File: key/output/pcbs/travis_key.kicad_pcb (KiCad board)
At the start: 2 copper layers, 38.1 x 38.1 mm, 4 parts

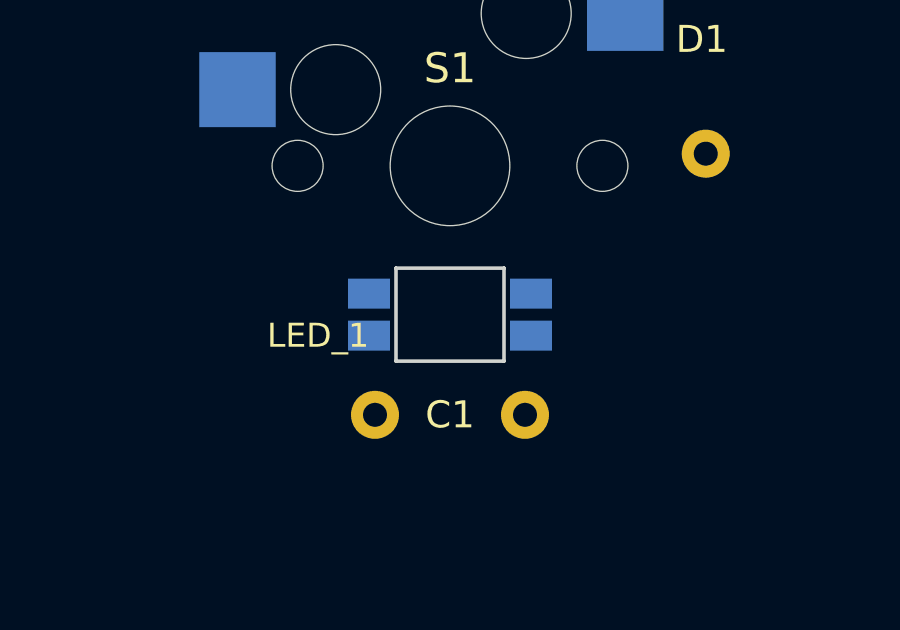
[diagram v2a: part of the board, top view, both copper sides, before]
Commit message: rtl option added
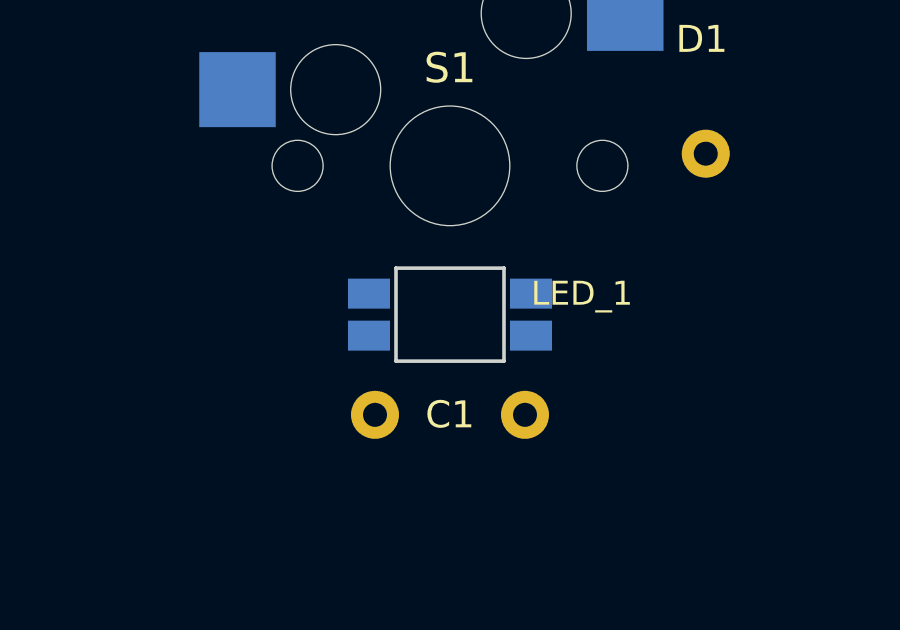
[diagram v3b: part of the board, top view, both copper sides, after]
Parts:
- moved C1 5.00 mm to (-2.50, 8.30), turned to 0 degrees
- turned LED1 to 180 degrees
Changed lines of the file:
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@@
       (module "ceoloide:led_SK6812mini-e (per-key single-side)"
         (layer B.Cu)
-        (at 0 4.96 0)
-        (fp_text reference "LED1" (at -5.25 0 90) (layer B.SilkS)
+        (at 0 4.96 180)
+        (fp_text reference "LED1" (at -4.75 0 270) (layer B.SilkS)
           (effects (font (size 1 1) (thickness 0.15)) (justify  mirror))
         )
-        (fp_text value "SK6812mini-e" (at 0 -2.25 0) (layer "B.Fab")
+        (fp_text value "SK6812mini-e" (at 0 2.25 180) (layer "B.Fab")
           (effects (font (size 0.8 0.8) (thickness 0.15)))
         )
@@
         (fp_line (start -3.8 0) (end -3.8 -1.6) (layer B.SilkS) (width 0.12))
         (fp_line (start -3.8 -1.36) (end -3.56 -1.6) (layer B.SilkS) (width 0.12))
-        (pad 2 smd rect (at 2.70 -0.7 0) (size 1.4 1) (layers B.Cu B.Paste B.Mask) (net 5 "LED_2"))
-        (pad 1 smd rect (at 2.70 0.7 0) (size 1.4 1) (layers B.Cu B.Paste B.Mask) (net 4 "RAW"))
-        (pad 3 smd rect (at -2.70 -0.7 0) (size 1.4 1) (layers B.Cu B.Paste B.Mask) (net 6 "GND"))
-        (pad 4 smd rect (at -2.70 0.7 0) (size 1.4 1) (layers B.Cu B.Paste B.Mask) (net 7 "LED_1"))
+        (pad 2 smd rect (at 2.70 -0.7 180) (size 1.4 1) (layers B.Cu B.Paste B.Mask) (net 5 "LED_2"))
+        (pad 1 smd rect (at 2.70 0.7 180) (size 1.4 1) (layers B.Cu B.Paste B.Mask) (net 4 "RAW"))
+        (pad 3 smd rect (at -2.70 -0.7 180) (size 1.4 1) (layers B.Cu B.Paste B.Mask) (net 6 "GND"))
+        (pad 4 smd rect (at -2.70 0.7 180) (size 1.4 1) (layers B.Cu B.Paste B.Mask) (net 7 "LED_1"))
     (fp_line (start -0.8 -1.4) (end -0.8 1.4) (layer Dwgs.User) (width 0.12))
     (fp_line (start 0.8 -1.4) (end 0.8 1.4) (layer Dwgs.User) (width 0.12))
@@
         (polygon
           (pts
+            (xy 2.000 6.810)
+            (xy -2.000 6.810)
             (xy -2.000 3.110)
             (xy 2.000 3.110)
-            (xy 2.000 6.810)
-            (xy -2.000 6.810)
           )
         )
       )
-      (gr_text "LED_1" (at -2.7 5.66 0) (layer F.SilkS)
-        (effects (font (size 0.8 0.8) (thickness 0.15)) (justify right))
+      (gr_text "LED_1" (at 2.7 4.26 0) (layer F.SilkS)
+        (effects (font (size 0.8 0.8) (thickness 0.15)) (justify left))
       )
     (module C_Disc_D4.7mm_W2.5mm_P5.00mm (layer B.Cu)
     (descr "C, Disc series, Radial, pin pitch=5.00mm, , diameter*width=4.7*2.5mm^2, Capacitor, http://www.vishay.com/docs/45233/krseries.pdf")
     (tags "C Disc series Radial pin pitch 5.00mm  diameter 4.7mm width 2.5mm Capacitor")
-    (at 2.5 8.3 180)
-    (fp_text reference "C1" (at 7.5 0 180) (layer B.SilkS)
+    (at -2.5 8.3 0)
+    (fp_text reference "C1" (at 7.5 0 0) (layer B.SilkS)
       (effects (font (size 1 1) (thickness 0.15)) (justify mirror))
     )
-    (fp_text value "104" (at -2.5 0 180) (layer B.Fab)
+    (fp_text value "104" (at -2.5 0 0) (layer B.Fab)
       (effects (font (size 1 1) (thickness 0.15)))
     )

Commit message: footprint updates
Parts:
- C1: footprint C_Disc_D4.7mm_W2.5mm_P5.00mm -> travis:C_Disc_D4.7mm_W2.5mm_P5.00mm
- D1: footprint Diode_DO-35 -> travis:Diode_DO-35
- LED1: footprint ceoloide:led_SK6812mini-e (per-key single-side) -> travis:led_SK6812mini-e (per-key single-side)
- S1: footprint MX -> travis:MX
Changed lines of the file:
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@@
 (add_net "LED_1")
   )
-        (module MX (layer F.Cu)
+        (module "travis:MX" (layer F.Cu)
         (at 0 0 0)
         (fp_text reference "S1" (at 0 -3.25) (layer F.SilkS)  (effects (font (size 1 1) (thickness 0.15))))
@@
 		(rotate (xyz 0 0 0) )
 	  ))
-    (module "Diode_DO-35" (layer "B.Cu")
+    (module "travis:Diode_DO-35" (layer "B.Cu")
     (descr "Diode, DO-35_SOD27 series, Axial, Horizontal, pin pitch=7.62mm, , length*diameter=4*2mm^2, , http://www.diodes.com/_files/packages/DO-35.pdf")
     (tags "Diode DO-35_SOD27 series Axial Horizontal pin pitch 7.62mm  length 4mm diameter 2mm")
@@
         (effects (font (size 0.9 0.9) (thickness 0.15)) (justify left))
       )
-      (module "ceoloide:led_SK6812mini-e (per-key single-side)"
+      (module "travis:led_SK6812mini-e (per-key single-side)"
         (layer B.Cu)
         (at 0 4.96 180)
@@
         (effects (font (size 0.8 0.8) (thickness 0.15)) (justify left))
       )
-    (module C_Disc_D4.7mm_W2.5mm_P5.00mm (layer B.Cu)
+    (module "travis:C_Disc_D4.7mm_W2.5mm_P5.00mm" (layer B.Cu)
     (descr "C, Disc series, Radial, pin pitch=5.00mm, , diameter*width=4.7*2.5mm^2, Capacitor, http://www.vishay.com/docs/45233/krseries.pdf")
     (tags "C Disc series Radial pin pitch 5.00mm  diameter 4.7mm width 2.5mm Capacitor")

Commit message: footprint/module updates
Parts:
- C1: footprint travis:C_Disc_D4.7mm_W2.5mm_P5.00mm -> Capacitor_THT:C_Disc_D4.7mm_W2.5mm_P5.00mm
- D1: footprint travis:Diode_DO-35 -> ScottoKeebs_Components:Diode_DO-35
- LED1: footprint travis:led_SK6812mini-e (per-key single-side) -> travis:led_SK6812mini-e (per-key, single-side)
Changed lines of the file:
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@@
 		(rotate (xyz 0 0 0) )
 	  ))
-    (module "travis:Diode_DO-35" (layer "B.Cu")
+    (module "ScottoKeebs_Components:Diode_DO-35" (layer "B.Cu")
     (descr "Diode, DO-35_SOD27 series, Axial, Horizontal, pin pitch=7.62mm, , length*diameter=4*2mm^2, , http://www.diodes.com/_files/packages/DO-35.pdf")
     (tags "Diode DO-35_SOD27 series Axial Horizontal pin pitch 7.62mm  length 4mm diameter 2mm")
@@
         (effects (font (size 0.9 0.9) (thickness 0.15)) (justify left))
       )
-      (module "travis:led_SK6812mini-e (per-key single-side)"
+      (module "travis:led_SK6812mini-e (per-key, single-side)"
         (layer B.Cu)
         (at 0 4.96 180)
@@
         (effects (font (size 0.8 0.8) (thickness 0.15)) (justify left))
       )
-    (module "travis:C_Disc_D4.7mm_W2.5mm_P5.00mm" (layer B.Cu)
+    (module "Capacitor_THT:C_Disc_D4.7mm_W2.5mm_P5.00mm" (layer B.Cu)
     (descr "C, Disc series, Radial, pin pitch=5.00mm, , diameter*width=4.7*2.5mm^2, Capacitor, http://www.vishay.com/docs/45233/krseries.pdf")
     (tags "C Disc series Radial pin pitch 5.00mm  diameter 4.7mm width 2.5mm Capacitor")
